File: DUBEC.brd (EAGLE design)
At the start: 40 x 21.4 mm, 70 parts

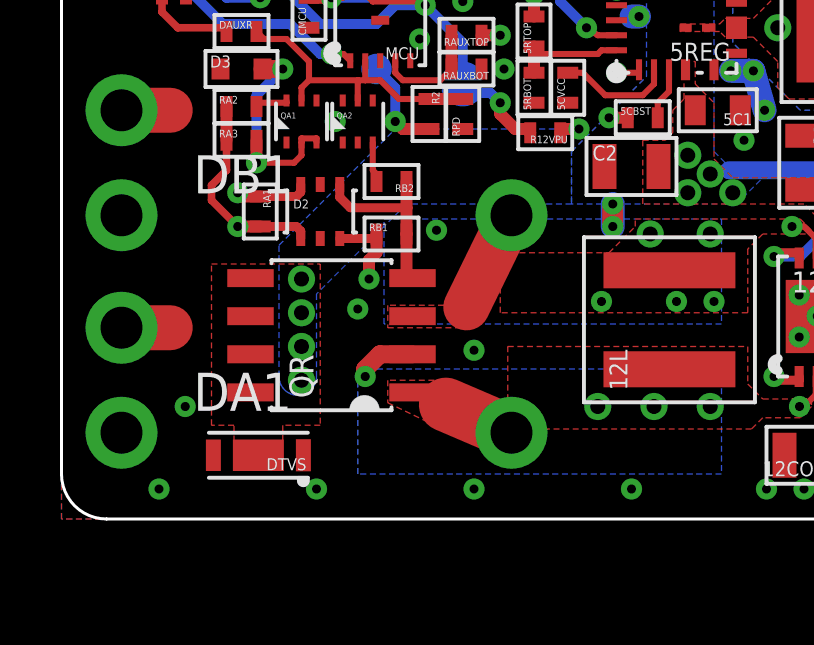
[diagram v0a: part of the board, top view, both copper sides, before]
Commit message: Gate bias from source
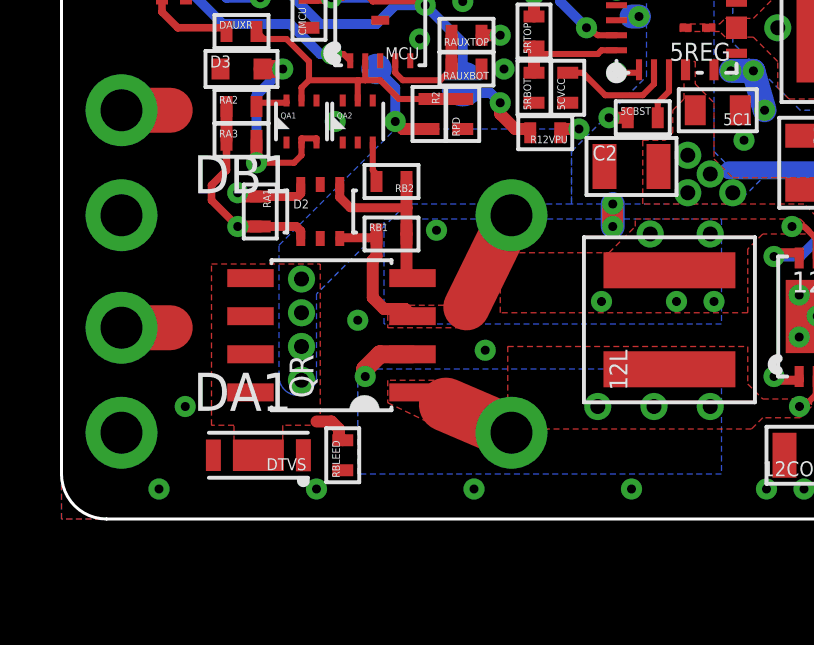
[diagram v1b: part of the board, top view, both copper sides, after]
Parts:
- added RBLEED: RES40.2K_16, dubec:0402
- RA1, RB1: value RES10K_16 -> RES40.2K_16
- RA2, RB2: value RES5.9K_16 -> RES10K_16
- RA3: value RES200K_16 -> RES1M_16
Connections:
- net 35V: now also RBLEED.2
- net BATT_AUX: no longer D2.3, RB1.1
- net BATT_MAIN: no longer D2.6, RA1.1
- net GND: now also RBLEED.1
- net N$6: now also D2.6, RA1.1
- net N$8: now also D2.3, RB1.1
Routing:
- net N$6: track 2.38 -> 17.7 mm, vias 0 -> 1
- net BATT_MAIN: track 12.1 -> 0.00 mm, vias 1 -> 0
- net BATT_AUX: track 24.9 -> 15.7 mm, vias 2 -> 1
- net N$8: track 3.41 -> 8.45 mm
- net 35V: track 38.9 -> 40.1 mm

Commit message: tidy
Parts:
- removed RBLEED: RES40.2K_16, dubec:0402
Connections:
- net 35V: no longer RBLEED.2
- net GND: no longer RBLEED.1
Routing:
- net 35V: track 40.1 -> 38.9 mm
- net 12V_RUN: track 18.1 -> 18.8 mm
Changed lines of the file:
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@@
 <attribute name="MFG_PART_#" value="C2012X5R1A476M125AC" x="34.6875" y="15.3125" size="1.778" layer="27" rot="R270" display="off"/>
-</element>
-<element name="RBLEED" library="dubec" package="0402" value="RES40.2K_16" x="9.375" y="2.125" rot="R90">
-<attribute name="DIGIKEY_PART_#" value="541-40.2KLCT-ND" x="9.375" y="2.125" size="1.778" layer="27" rot="R90" display="off"/>
-<attribute name="MFG_PART_#" value="CRCW040240K2FKED" x="9.375" y="2.125" size="1.778" layer="27" rot="R90" display="off"/>
-<attribute name="TEMP" value="±100ppm/°C" x="9.375" y="2.125" size="1.778" layer="27" rot="R90" display="off"/>
-<attribute name="USD" value="2.11/50" x="9.375" y="2.125" size="1.778" layer="27" rot="R90" display="off"/>
-<attribute name="TOLERANCE" value="±1%" x="9.375" y="2.125" size="1.778" layer="27" rot="R90" display="off"/>
-<attribute name="MANUFACTURER" value="Vishay Dale" x="9.375" y="2.125" size="1.778" layer="27" rot="R90" display="off"/>
 </element>
 </elements>
@@
 <vertex x="20.25" y="18.625"/>
 <vertex x="19.8125" y="19.0625"/>
-<vertex x="19.8125" y="21.75"/>
-<vertex x="21.875" y="21.75"/>
+<vertex x="19.8125" y="21.375"/>
+<vertex x="21.875" y="21.375"/>
 <vertex x="21.875" y="20.125"/>
 <vertex x="21.5" y="19.75"/>
@@
 <via x="20.3125" y="20.3125" extent="1-16" drill="0.5"/>
 <polygon width="0.3302" layer="16" isolate="0.3302" thermals="no">
-<vertex x="19.5" y="21.75"/>
-<vertex x="21.75" y="21.75"/>
+<vertex x="19.5" y="21.375"/>
+<vertex x="21.75" y="21.375"/>
 <vertex x="21.75" y="12.25"/>
 <vertex x="22.25" y="11.75"/>
@@
 <wire x1="21.625" y1="11.5" x2="22.375" y2="10.875" width="1" layer="2"/>
 <wire x1="22.375" y1="10.875" x2="20.875" y2="10.875" width="1" layer="2"/>
-<contactref element="RBLEED" pad="2"/>
-<wire x1="9.375" y1="2.625" x2="9.25" y2="2.75" width="0.4" layer="1"/>
-<wire x1="9.25" y1="2.75" x2="9.25" y2="3" width="0.4" layer="1"/>
-<wire x1="9.25" y1="3" x2="9" y2="3.25" width="0.4" layer="1"/>
-<wire x1="9" y1="3.25" x2="8.5" y2="3.25" width="0.4" layer="1"/>
 </signal>
 <signal name="12V_BST1">
@@
 <polygon width="0.2032" layer="1" thermals="no" rank="5">
 <vertex x="0" y="0"/>
-<vertex x="0" y="21.75"/>
-<vertex x="41" y="21.75"/>
-<vertex x="41" y="0"/>
+<vertex x="0" y="21.875"/>
+<vertex x="40.625" y="21.875"/>
+<vertex x="40.625" y="0"/>
 </polygon>
 <via x="24.59" y="7.465" extent="1-16" drill="0.3"/>
@@
 <contactref element="C1" pad="1"/>
 <polygon width="0.3302" layer="16" isolate="0.3302" rank="5">
-<vertex x="0" y="21.75"/>
-<vertex x="41" y="21.75"/>
-<vertex x="41" y="0"/>
+<vertex x="0" y="22.625"/>
+<vertex x="41.375" y="22.625"/>
+<vertex x="41.375" y="0"/>
 <vertex x="0" y="0"/>
 </polygon>
 <contactref element="C2" pad="1"/>
 <polygon width="0.2032" layer="15" spacing="0.254" isolate="0.3302" rank="5">
-<vertex x="0" y="21.75"/>
-<vertex x="41" y="21.75"/>
+<vertex x="0" y="22.25"/>
+<vertex x="41" y="22.25"/>
 <vertex x="41" y="0"/>
 <vertex x="0" y="0"/>
@@
 <via x="14.125" y="5.625" extent="1-16" drill="0.3"/>
 <via x="12.5" y="9.625" extent="1-16" drill="0.3"/>
-<contactref element="RBLEED" pad="1"/>
 </signal>
 <signal name="12V">
@@
 <vertex x="25.5" y="4.25"/>
 <vertex x="25.5" y="0"/>
-<vertex x="41" y="0"/>
-<vertex x="41" y="3.625"/>
+<vertex x="40" y="0"/>
+<vertex x="40" y="3.625"/>
 <vertex x="36.5" y="3.625"/>
 <vertex x="36.25" y="3.375"/>
@@
 <wire x1="24.5892" y1="4.625" x2="23.875" y2="4.625" width="0.3048" layer="1"/>
 <wire x1="23.875" y1="4.625" x2="23.75" y2="4.75" width="0.3048" layer="1"/>
-<wire x1="23.75" y1="4.75" x2="21.75" y2="4.75" width="0.3302" layer="15"/>
-<wire x1="21.75" y1="4.75" x2="17.5" y2="9" width="0.3302" layer="15"/>
+<wire x1="23.75" y1="4.75" x2="20.5" y2="4.75" width="0.3302" layer="15"/>
+<wire x1="20.5" y1="4.75" x2="16.75" y2="8.5" width="0.3302" layer="15"/>
 <contactref element="R12VPU" pad="2"/>
-<wire x1="17.5" y1="11" x2="14.625" y2="13.875" width="0.3302" layer="15"/>
-<wire x1="17.5" y1="11" x2="17.5" y2="9" width="0.3302" layer="15"/>
+<wire x1="16.75" y1="10.75" x2="14.625" y2="12.875" width="0.3302" layer="15"/>
+<wire x1="14.625" y1="12.875" x2="14.625" y2="13.875" width="0.3302" layer="15"/>
+<wire x1="16.75" y1="10.75" x2="16.75" y2="8.5" width="0.3302" layer="15"/>
 <contactref element="SJ1" pad="1"/>
 <wire x1="13.375" y1="14.2" x2="14.3" y2="14.2" width="0.3302" layer="16"/>
@@
 <wire x1="28.5" y1="11.625" x2="27.75" y2="11.5" width="0.8" layer="15" curve="28.072487"/>
 <wire x1="27.75" y1="11.5" x2="24.35" y2="9.75" width="0.8" layer="15"/>
-<via x="18" y="7.25" extent="1-16" drill="0.3"/>
+<via x="19.25" y="7.25" extent="1-16" drill="0.3"/>
 <via x="19.625" y="9.5" extent="1-16" drill="0.5"/>
 <wire x1="25.14" y1="8.7" x2="25.14" y2="9.36" width="0.2032" layer="1"/>
@@
 <via x="21.75" y="7.25" extent="1-16" drill="0.3"/>
 <via x="20.5" y="7.25" extent="1-16" drill="0.3"/>
-<wire x1="20.5" y1="7.25" x2="21.75" y2="7.25" width="0.7" layer="2"/>
 <wire x1="20.5" y1="7.25" x2="21.75" y2="7.25" width="0.7" layer="15"/>
+<wire x1="19.25" y1="7.25" x2="20.5" y2="7.25" width="0.7" layer="15"/>
 </signal>
 <signal name="12V_SW2">
@@
 <wire x1="5.875" y1="10.875" x2="6" y2="10.75" width="0.4" layer="1"/>
 <wire x1="6" y1="10.75" x2="6.625" y2="10.75" width="0.4" layer="1"/>
-<wire x1="5.875" y1="10.875" x2="7.625" y2="10.875" width="0.3302" layer="15"/>
-<wire x1="7.625" y1="10.875" x2="15" y2="3.5" width="0.3302" layer="15"/>
+<wire x1="5.875" y1="10.875" x2="6.25" y2="10.5" width="0.3302" layer="15"/>
+<wire x1="6.25" y1="10.5" x2="8" y2="10.5" width="0.3302" layer="15"/>
+<wire x1="8" y1="10.5" x2="15" y2="3.5" width="0.3302" layer="15"/>
 <wire x1="15" y1="3.5" x2="15" y2="2.875" width="0.3302" layer="15"/>
 <wire x1="11.7" y1="4.22" x2="12.8125" y2="3.8125" width="0" layer="19" extent="1-1"/>

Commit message: Upped switch resistors
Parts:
- RA1, RB1: value RES40.2K_16 -> RES90.9K_16
- RA2, RB2: value RES10K_16 -> RES40.2K_16
- RA3: value RES1M_16 -> RES2M_16
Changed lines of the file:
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@@
 <attribute name="TOLERANCE" value="±5%" x="8.625" y="10.25" size="1.778" layer="27" display="off"/>
 </element>
-<element name="RA2" library="dubec" package="0402" value="RES10K_16" x="6" y="13.75">
+<element name="RA2" library="dubec" package="0402" value="RES40.2K_16" x="6" y="13.75">
 <attribute name="TOLERANCE" value="±1%" x="6" y="13.75" size="1.778" layer="27" display="off"/>
 <attribute name="TEMP" value="±100ppm/°C" x="6" y="13.75" size="1.778" layer="27" display="off"/>
-<attribute name="DIGIKEY_PART_#" value="541-10.0KLCT-ND" x="6" y="13.75" size="1.778" layer="27" display="off"/>
+<attribute name="DIGIKEY_PART_#" value="541-40.2KLCT-ND" x="6" y="13.75" size="1.778" layer="27" display="off"/>
 <attribute name="MANUFACTURER" value="Vishay Dale" x="6" y="13.75" size="1.778" layer="27" display="off"/>
-<attribute name="MFG_PART_#" value="CRCW040210K0FKED" x="6" y="13.75" size="1.778" layer="27" display="off"/>
-<attribute name="EURO" value="2.10/50" x="6" y="13.75" size="1.778" layer="27" display="off"/>
+<attribute name="MFG_PART_#" value="CRCW040240K2FKED" x="6" y="13.75" size="1.778" layer="27" display="off"/>
+<attribute name="USD" value="2.11/50" x="6" y="13.75" size="1.778" layer="27" display="off"/>
 </element>
-<element name="RB2" library="dubec" package="0402" value="RES10K_16" x="11" y="11.25" rot="R180">
+<element name="RB2" library="dubec" package="0402" value="RES40.2K_16" x="11" y="11.25" rot="R180">
 <attribute name="TOLERANCE" value="±1%" x="11" y="11.25" size="1.778" layer="27" rot="R180" display="off"/>
 <attribute name="TEMP" value="±100ppm/°C" x="11" y="11.25" size="1.778" layer="27" rot="R180" display="off"/>
-<attribute name="DIGIKEY_PART_#" value="541-10.0KLCT-ND" x="11" y="11.25" size="1.778" layer="27" rot="R180" display="off"/>
+<attribute name="DIGIKEY_PART_#" value="541-40.2KLCT-ND" x="11" y="11.25" size="1.778" layer="27" rot="R180" display="off"/>
 <attribute name="MANUFACTURER" value="Vishay Dale" x="11" y="11.25" size="1.778" layer="27" rot="R180" display="off"/>
-<attribute name="MFG_PART_#" value="CRCW040210K0FKED" x="11" y="11.25" size="1.778" layer="27" rot="R180" display="off"/>
-<attribute name="EURO" value="2.10/50" x="11" y="11.25" size="1.778" layer="27" rot="R180" display="off"/>
+<attribute name="MFG_PART_#" value="CRCW040240K2FKED" x="11" y="11.25" size="1.778" layer="27" rot="R180" display="off"/>
+<attribute name="USD" value="2.11/50" x="11" y="11.25" size="1.778" layer="27" rot="R180" display="off"/>
 </element>
 <element name="QA1" library="dubec" package="SOT-666" value="2NMOS60V_0.2A" x="8" y="13.25">
@@
 <element name="GND_MAIN" library="dubec" package="1X01_NO_SILK" value="M01" x="2" y="13.625"/>
 <element name="GND_AUX" library="dubec" package="1X01_NO_SILK" value="M01" x="2" y="6.375"/>
-<element name="RA1" library="dubec" package="0402" value="RES40.2K_16" x="6.625" y="10.25" rot="R270">
+<element name="RA1" library="dubec" package="0402" value="RES90.9K_16" x="6.625" y="10.25" rot="R270">
 <attribute name="TOLERANCE" value="±1%" x="6.625" y="10.25" size="1.778" layer="27" rot="R270" display="off"/>
 <attribute name="TEMP" value="±100ppm/°C" x="6.625" y="10.25" size="1.778" layer="27" rot="R270" display="off"/>
-<attribute name="DIGIKEY_PART_#" value="541-40.2KLCT-ND" x="6.625" y="10.25" size="1.778" layer="27" rot="R270" display="off"/>
+<attribute name="DIGIKEY_PART_#" value="541-90.9KLCT-ND" x="6.625" y="10.25" size="1.778" layer="27" rot="R270" display="off"/>
 <attribute name="MANUFACTURER" value="Vishay Dale" x="6.625" y="10.25" size="1.778" layer="27" rot="R270" display="off"/>
-<attribute name="MFG_PART_#" value="CRCW040240K2FKED" x="6.625" y="10.25" size="1.778" layer="27" rot="R270" display="off"/>
-<attribute name="USD" value="2.11/50" x="6.625" y="10.25" size="1.778" layer="27" rot="R270" display="off"/>
+<attribute name="MFG_PART_#" value="CRCW040290K9FKED" x="6.625" y="10.25" size="1.778" layer="27" rot="R270" display="off"/>
+<attribute name="USD" value="0.78/10" x="6.625" y="10.25" size="1.778" layer="27" rot="R270" display="off"/>
 </element>
-<element name="RB1" library="dubec" package="0402" value="RES40.2K_16" x="11" y="9.5">
+<element name="RB1" library="dubec" package="0402" value="RES90.9K_16" x="11" y="9.5">
 <attribute name="TOLERANCE" value="±1%" x="11" y="9.5" size="1.778" layer="27" display="off"/>
 <attribute name="TEMP" value="±100ppm/°C" x="11" y="9.5" size="1.778" layer="27" display="off"/>
-<attribute name="DIGIKEY_PART_#" value="541-40.2KLCT-ND" x="11" y="9.5" size="1.778" layer="27" display="off"/>
+<attribute name="DIGIKEY_PART_#" value="541-90.9KLCT-ND" x="11" y="9.5" size="1.778" layer="27" display="off"/>
 <attribute name="MANUFACTURER" value="Vishay Dale" x="11" y="9.5" size="1.778" layer="27" display="off"/>
-<attribute name="MFG_PART_#" value="CRCW040240K2FKED" x="11" y="9.5" size="1.778" layer="27" display="off"/>
-<attribute name="USD" value="2.11/50" x="11" y="9.5" size="1.778" layer="27" display="off"/>
+<attribute name="MFG_PART_#" value="CRCW040290K9FKED" x="11" y="9.5" size="1.778" layer="27" display="off"/>
+<attribute name="USD" value="0.78/10" x="11" y="9.5" size="1.778" layer="27" display="off"/>
 </element>
-<element name="RA3" library="dubec" package="0402" value="RES1M_16" x="6" y="12.625">
+<element name="RA3" library="dubec" package="0402" value="RES2M_16" x="6" y="12.625">
 <attribute name="TOLERANCE" value="±1%" x="6" y="12.625" size="1.778" layer="27" display="off"/>
 <attribute name="TEMP" value="±100ppm/°C" x="6" y="12.625" size="1.778" layer="27" display="off"/>
-<attribute name="DIGIKEY_PART_#" value="541-1.00MLCT-ND" x="6" y="12.625" size="1.778" layer="27" display="off"/>
+<attribute name="DIGIKEY_PART_#" value="541-2.00MLCT-ND" x="6" y="12.625" size="1.778" layer="27" display="off"/>
 <attribute name="MANUFACTURER" value="Vishay Dale" x="6" y="12.625" size="1.778" layer="27" display="off"/>
-<attribute name="MFG_PART_#" value="CRCW04021M00FKED" x="6" y="12.625" size="1.778" layer="27" display="off"/>
-<attribute name="USD" value="2.11/50" x="6" y="12.625" size="1.778" layer="27" display="off"/>
+<attribute name="MFG_PART_#" value="CRCW04022M00FKED" x="6" y="12.625" size="1.778" layer="27" display="off"/>
+<attribute name="EURO" value="2.01/50" x="6" y="12.625" size="1.778" layer="27" display="off"/>
 </element>
 <element name="QA2" library="dubec" package="SOT-666" value="2NMOS60V_0.2A" x="9.875" y="13.25">

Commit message: Tweaks
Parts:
- moved D3 3.12 mm to (6.00, 11.9)
- moved AUX_OUT 1.19 mm to (10.1, 13.9)
- moved RA2 0.50 mm to (6.00, 14.2)
- moved RA3 0.50 mm to (6.00, 13.1)
- moved RA1 0.38 mm to (6.62, 9.88)
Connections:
- net N$6 renamed SRC_MAIN
- net N$8 renamed SRC_AUX
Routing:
- net GND: track 22.4 -> 26.2 mm, vias 44 -> 46
- net GATE_MAIN_B: track 7.72 -> 4.05 mm, vias 2 -> 0
- net GATE_MAIN: track 16.9 -> 18.1 mm, vias 2 -> 3
- net TP_AUX: track 3.24 -> 2.49 mm
